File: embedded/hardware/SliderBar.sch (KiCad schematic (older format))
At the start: 35 parts, among them J1 USB_B_Mini, J2 MOTOR_OUT, J3 POT_IN, J4 DEBUG, U1 MIC5205-3.3YM5, U2 TB6612FNG, U3 MT3608, U4 STM32F072C8Tx

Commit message: Change connector footprints to JST GH 1.25mm
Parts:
- J2: footprint Connector_JST:JST_GH_SM02B-GHS-TB_1x02-1MP_P1.25mm_Horizontal -> Connector_Molex:Molex_PicoBlade_53048-0210_1x02_P1.25mm_Horizontal
- J3: footprint Connector_JST:JST_GH_SM03B-GHS-TB_1x03-1MP_P1.25mm_Horizontal -> Connector_Molex:Molex_PicoBlade_53048-0310_1x03_P1.25mm_Horizontal
- J4: footprint Connector_JST:JST_GH_SM05B-GHS-TB_1x05-1MP_P1.25mm_Horizontal -> Connector_Molex:Molex_PicoBlade_53047-0510_1x05_P1.25mm_Vertical
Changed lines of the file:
@@
 F 0 "J4" H 4230 4292 50  0000 L CNN
 F 1 "DEBUG" H 4230 4201 50  0000 L CNN
-F 2 "Connector_JST:JST_GH_SM05B-GHS-TB_1x05-1MP_P1.25mm_Horizontal" H 4150 4250 50  0001 C CNN
+F 2 "Connector_Molex:Molex_PicoBlade_53047-0510_1x05_P1.25mm_Vertical" H 4150 4250 50  0001 C CNN
 F 3 "~" H 4150 4250 50  0001 C CNN
 	1    4150 4250
@@
 F 0 "J2" H 4230 3092 50  0000 L CNN
 F 1 "MOTOR_OUT" H 4230 3001 50  0000 L CNN
-F 2 "Connector_JST:JST_GH_SM02B-GHS-TB_1x02-1MP_P1.25mm_Horizontal" H 4150 3100 50  0001 C CNN
+F 2 "Connector_Molex:Molex_PicoBlade_53048-0210_1x02_P1.25mm_Horizontal" H 4150 3100 50  0001 C CNN
 F 3 "~" H 4150 3100 50  0001 C CNN
 	1    4150 3100
@@
 F 0 "J3" H 4230 3667 50  0000 L CNN
 F 1 "POT_IN" H 4230 3576 50  0000 L CNN
-F 2 "Connector_JST:JST_GH_SM03B-GHS-TB_1x03-1MP_P1.25mm_Horizontal" H 4150 3625 50  0001 C CNN
+F 2 "Connector_Molex:Molex_PicoBlade_53048-0310_1x03_P1.25mm_Horizontal" H 4150 3625 50  0001 C CNN
 F 3 "~" H 4150 3625 50  0001 C CNN
 	1    4150 3625
@@
 NRST
 $Comp
-L power:GND #PWR018
+L power:GND #PWR?
 U 1 1 5BB23C60
 P 3950 4150
-F 0 "#PWR018" H 3950 3900 50  0001 C CNN
+F 0 "#PWR?" H 3950 3900 50  0001 C CNN
 F 1 "GND" V 3950 4000 50  0000 R CNN
 F 2 "" H 3950 4150 50  0001 C CNN
@@
 POT
 $Comp
-L power:GND #PWR020
+L power:GND #PWR?
 U 1 1 5BB24025
 P 3950 3725
-F 0 "#PWR020" H 3950 3475 50  0001 C CNN
+F 0 "#PWR?" H 3950 3475 50  0001 C CNN
 F 1 "GND" H 3955 3552 50  0000 C CNN
 F 2 "" H 3950 3725 50  0001 C CNN
@@
 $EndComp
 $Comp
-L power:+3.3V #PWR019
+L power:+3.3V #PWR?
 U 1 1 5BB24078
 P 3950 3525
-F 0 "#PWR019" H 3950 3375 50  0001 C CNN
+F 0 "#PWR?" H 3950 3375 50  0001 C CNN
 F 1 "+3.3V" H 3965 3698 50  0000 C CNN
 F 2 "" H 3950 3525 50  0001 C CNN
@@
 $EndComp
 $Comp
-L power:GND #PWR05
+L power:GND #PWR?
 U 1 1 5BB24638
 P 9350 6050
-F 0 "#PWR05" H 9350 5800 50  0001 C CNN
+F 0 "#PWR?" H 9350 5800 50  0001 C CNN
 F 1 "GND" H 9355 5877 50  0000 C CNN
 F 2 "" H 9350 6050 50  0001 C CNN
@@
 MOT_IN_PWM
 $Comp
-L power:+10V #PWR07
+L power:+10V #PWR?
 U 1 1 5BB2664B
 P 9950 3450
-F 0 "#PWR07" H 9950 3300 50  0001 C CNN
+F 0 "#PWR?" H 9950 3300 50  0001 C CNN
 F 1 "+10V" H 9965 3623 50  0000 C CNN
 F 2 "" H 9950 3450 50  0001 C CNN
@@
 	9750 3900 9750 3950
 $Comp
-L power:+3V3 #PWR04
+L power:+3V3 #PWR?
 U 1 1 5BB27786
 P 9350 3950
-F 0 "#PWR04" H 9350 3800 50  0001 C CNN
+F 0 "#PWR?" H 9350 3800 50  0001 C CNN
 F 1 "+3V3" H 9300 4100 50  0000 C CNN
 F 2 "" H 9350 3950 50  0001 C CNN
@@
 MOT_IN_2
 $Comp
-L power:GND #PWR010
+L power:GND #PWR?
 U 1 1 5BB27E3D
 P 10400 4000
-F 0 "#PWR010" H 10400 3750 50  0001 C CNN
+F 0 "#PWR?" H 10400 3750 50  0001 C CNN
 F 1 "GND" V 10405 3872 50  0000 R CNN
 F 2 "" H 10400 4000 50  0001 C CNN
@@
 Connection ~ 9950 3900
 $Comp
-L power:+3V3 #PWR016
+L power:+3V3 #PWR?
 U 1 1 5BCA2B2D
 P 6750 1900
-F 0 "#PWR016" H 6750 1750 50  0001 C CNN
+F 0 "#PWR?" H 6750 1750 50  0001 C CNN
 F 1 "+3V3" H 6765 2073 50  0000 C CNN
 F 2 "" H 6750 1900 50  0001 C CNN
@@
 Connection ~ 6650 2000
 $Comp
-L power:GND #PWR015
+L power:GND #PWR?
 U 1 1 5BCAB682
 P 6550 5300
-F 0 "#PWR015" H 6550 5050 50  0001 C CNN
+F 0 "#PWR?" H 6550 5050 50  0001 C CNN
 F 1 "GND" H 6555 5127 50  0000 C CNN
 F 2 "" H 6550 5300 50  0001 C CNN
@@
 Connection ~ 6850 2000
 $Comp
-L power:GND #PWR014
+L power:GND #PWR?
 U 1 1 5BCB754A
 P 5500 2700
-F 0 "#PWR014" H 5500 2450 50  0001 C CNN
+F 0 "#PWR?" H 5500 2450 50  0001 C CNN
 F 1 "GND" H 5505 2527 50  0000 C CNN
 F 2 "" H 5500 2700 50  0001 C CNN
@@
 	2050 1800 2050 1700
 $Comp
-L power:GND #PWR06
+L power:GND #PWR?
 U 1 1 5BD40D38
 P 2050 1800
-F 0 "#PWR06" H 2050 1550 50  0001 C CNN
+F 0 "#PWR?" H 2050 1550 50  0001 C CNN
 F 1 "GND" H 2055 1627 50  0000 C CNN
 F 2 "" H 2050 1800 50  0001 C CNN
@@
 $EndComp
 $Comp
-L power:+3V3 #PWR03
+L power:+3V3 #PWR?
 U 1 1 5BCA296C
 P 1900 1200
-F 0 "#PWR03" H 1900 1050 50  0001 C CNN
+F 0 "#PWR?" H 1900 1050 50  0001 C CNN
 F 1 "+3V3" H 1915 1373 50  0000 C CNN
 F 2 "" H 1900 1200 50  0001 C CNN
@@
 3.3V REGULATOR
 $Comp
-L power:GND #PWR02
+L power:GND #PWR?
 U 1 1 5BC34408
 P 1500 2000
-F 0 "#PWR02" H 1500 1750 50  0001 C CNN
+F 0 "#PWR?" H 1500 1750 50  0001 C CNN
 F 1 "GND" H 1505 1827 50  0000 C CNN
 F 2 "" H 1500 2000 50  0001 C CNN
@@
 Id = sqrt(Iout * Imax)
 $Comp
-L power:GND #PWR012
+L power:GND #PWR?
 U 1 1 5BC4D897
 P 2850 3850
-F 0 "#PWR012" H 2850 3600 50  0001 C CNN
+F 0 "#PWR?" H 2850 3600 50  0001 C CNN
 F 1 "GND" H 2855 3677 50  0000 C CNN
 F 2 "" H 2850 3850 50  0001 C CNN
@@
 Recommended:\n4.7uH - 22uH
 $Comp
-L power:GND #PWR011
+L power:GND #PWR?
 U 1 1 5BC48783
 P 2150 4450
-F 0 "#PWR011" H 2150 4200 50  0001 C CNN
+F 0 "#PWR?" H 2150 4200 50  0001 C CNN
 F 1 "GND" H 2155 4277 50  0000 C CNN
 F 2 "" H 2150 4450 50  0001 C CNN
@@
 $EndComp
 $Comp
-L power:+10V #PWR013
+L power:+10V #PWR?
 U 1 1 5BC3AC64
 P 2850 3250
-F 0 "#PWR013" H 2850 3100 50  0001 C CNN
+F 0 "#PWR?" H 2850 3100 50  0001 C CNN
 F 1 "+10V" H 2865 3423 50  0000 C CNN
 F 2 "" H 2850 3250 50  0001 C CNN
@@
 $EndComp
 $Comp
-L power:GND #PWR09
+L power:GND #PWR?
 U 1 1 5BC3A8CB
 P 900 4050
-F 0 "#PWR09" H 900 3800 50  0001 C CNN
+F 0 "#PWR?" H 900 3800 50  0001 C CNN
 F 1 "GND" H 905 3877 50  0000 C CNN
 F 2 "" H 900 4050 50  0001 C CNN
@@
 Connection ~ 9950 3550
 $Comp
-L power:+5V #PWR017
+L power:+5V #PWR?
 U 1 1 5BD9F21E
 P 1100 1200
-F 0 "#PWR017" H 1100 1050 50  0001 C CNN
+F 0 "#PWR?" H 1100 1050 50  0001 C CNN
 F 1 "+5V" H 1115 1373 50  0000 C CNN
 F 2 "" H 1100 1200 50  0001 C CNN
@@
 $EndComp
 $Comp
-L power:+5V #PWR01
+L power:+5V #PWR?
 U 1 1 5BD9F4E9
 P 900 3250
-F 0 "#PWR01" H 900 3100 50  0001 C CNN
+F 0 "#PWR?" H 900 3100 50  0001 C CNN
 F 1 "+5V" H 915 3423 50  0000 C CNN
 F 2 "" H 900 3250 50  0001 C CNN
@@
 $EndComp
 $Comp
-L power:VBUS #PWR023
+L power:VBUS #PWR?
 U 1 1 5BD9F98D
 P 3000 1300
-F 0 "#PWR023" H 3000 1150 50  0001 C CNN
+F 0 "#PWR?" H 3000 1150 50  0001 C CNN
 F 1 "VBUS" H 3015 1473 50  0000 C CNN
 F 2 "" H 3000 1300 50  0001 C CNN
@@
 $EndComp
 $Comp
-L power:+5V #PWR027
+L power:+5V #PWR?
 U 1 1 5BD9FC3F
 P 3750 1200
-F 0 "#PWR027" H 3750 1050 50  0001 C CNN
+F 0 "#PWR?" H 3750 1050 50  0001 C CNN
 F 1 "+5V" H 3765 1373 50  0000 C CNN
 F 2 "" H 3750 1200 50  0001 C CNN
@@
 $EndComp
 $Comp
-L power:GND #PWR028
+L power:GND #PWR?
 U 1 1 5BDBF2FB
 P 3750 2200
-F 0 "#PWR028" H 3750 1950 50  0001 C CNN
+F 0 "#PWR?" H 3750 1950 50  0001 C CNN
 F 1 "GND" H 3755 2027 50  0000 C CNN
 F 2 "" H 3750 2200 50  0001 C CNN
@@
 USB_DP
 $Comp
-L power:GND #PWR08
+L power:GND #PWR?
 U 1 1 5BDDF695
 P 950 6400
-F 0 "#PWR08" H 950 6150 50  0001 C CNN
+F 0 "#PWR?" H 950 6150 50  0001 C CNN
 F 1 "GND" H 955 6227 50  0000 C CNN
 F 2 "" H 950 6400 50  0001 C CNN
@@
 Connection ~ 10400 3900
 $Comp
-L power:VPP #PWR029
+L power:VPP #PWR?
 U 1 1 5BD8AB17
 P 3950 4350
-F 0 "#PWR029" H 3950 4200 50  0001 C CNN
+F 0 "#PWR?" H 3950 4200 50  0001 C CNN
 F 1 "VPP" V 3950 4650 50  0000 R CNN
 F 2 "" H 3950 4350 50  0001 C CNN
@@
 $EndComp
 $Comp
-L power:VPP #PWR024
+L power:VPP #PWR?
 U 1 1 5BD8AD8C
 P 3000 1650
-F 0 "#PWR024" H 3000 1500 50  0001 C CNN
+F 0 "#PWR?" H 3000 1500 50  0001 C CNN
 F 1 "VPP" H 3015 1823 50  0000 C CNN
 F 2 "" H 3000 1650 50  0001 C CNN
@@
 	4750 2700 3400 2700
 $Comp
-L power:VBUS #PWR021
+L power:VBUS #PWR?
 U 1 1 5BE0AEED
 P 1450 5500
-F 0 "#PWR021" H 1450 5350 50  0001 C CNN
+F 0 "#PWR?" H 1450 5350 50  0001 C CNN
 F 1 "VBUS" H 1465 5673 50  0000 C CNN
 F 2 "" H 1450 5500 50  0001 C CNN
@@
 Connection ~ 1050 6300
 $Comp
-L power:+3V3 #PWR022
+L power:+3V3 #PWR?
 U 1 1 5BE2449C
 P 1750 5400
-F 0 "#PWR022" H 1750 5250 50  0001 C CNN
+F 0 "#PWR?" H 1750 5250 50  0001 C CNN
 F 1 "+3V3" H 1765 5573 50  0000 C CNN
 F 2 "" H 1750 5400 50  0001 C CNN
@@
 	10900 2950 10900 6300
 $Comp
-L power:+3V3 #PWR025
+L power:+3V3 #PWR?
 U 1 1 5BE61DFB
 P 3650 6800
-F 0 "#PWR025" H 3650 6650 50  0001 C CNN
+F 0 "#PWR?" H 3650 6650 50  0001 C CNN
 F 1 "+3V3" H 3665 6973 50  0000 C CNN
 F 2 "" H 3650 6800 50  0001 C CNN
@@
 $EndComp
 $Comp
-L power:GND #PWR026
+L power:GND #PWR?
 U 1 1 5BE61E6A
 P 3650 7400
-F 0 "#PWR026" H 3650 7150 50  0001 C CNN
+F 0 "#PWR?" H 3650 7150 50  0001 C CNN
 F 1 "GND" H 3655 7227 50  0000 C CNN
 F 2 "" H 3650 7400 50  0001 C CNN
@@
 $EndComp
 $Comp
-L power:GND #PWR031
+L power:GND #PWR?
 U 1 1 5BE61EC4
 P 5500 7400
-F 0 "#PWR031" H 5500 7150 50  0001 C CNN
+F 0 "#PWR?" H 5500 7150 50  0001 C CNN
 F 1 "GND" H 5505 7227 50  0000 C CNN
 F 2 "" H 5500 7400 50  0001 C CNN
@@
 $EndComp
 $Comp
-L power:GND #PWR034
+L power:GND #PWR?
 U 1 1 5BE61F1E
 P 6150 7400
-F 0 "#PWR034" H 6150 7150 50  0001 C CNN
+F 0 "#PWR?" H 6150 7150 50  0001 C CNN
 F 1 "GND" H 6155 7227 50  0000 C CNN
 F 2 "" H 6150 7400 50  0001 C CNN
@@
 $EndComp
 $Comp
-L power:+5V #PWR030
+L power:+5V #PWR?
 U 1 1 5BE6210E
 P 5500 6800
-F 0 "#PWR030" H 5500 6650 50  0001 C CNN
+F 0 "#PWR?" H 5500 6650 50  0001 C CNN
 F 1 "+5V" H 5515 6973 50  0000 C CNN
 F 2 "" H 5500 6800 50  0001 C CNN
@@
 $EndComp
 $Comp
-L power:+10V #PWR033
+L power:+10V #PWR?
 U 1 1 5BE621BC
 P 6150 6800
-F 0 "#PWR033" H 6150 6650 50  0001 C CNN
+F 0 "#PWR?" H 6150 6650 50  0001 C CNN
 F 1 "+10V" H 6165 6973 50  0000 C CNN
 F 2 "" H 6150 6800 50  0001 C CNN
@@
 NOT NEEDED
 $Comp
-L power:GND #PWR032
+L power:GND #PWR?
 U 1 1 5BEDB912
 P 5850 2900
-F 0 "#PWR032" H 5850 2650 50  0001 C CNN
+F 0 "#PWR?" H 5850 2650 50  0001 C CNN
 F 1 "GND" H 5855 2727 50  0000 C CNN
 F 2 "" H 5850 2900 50  0001 C CNN

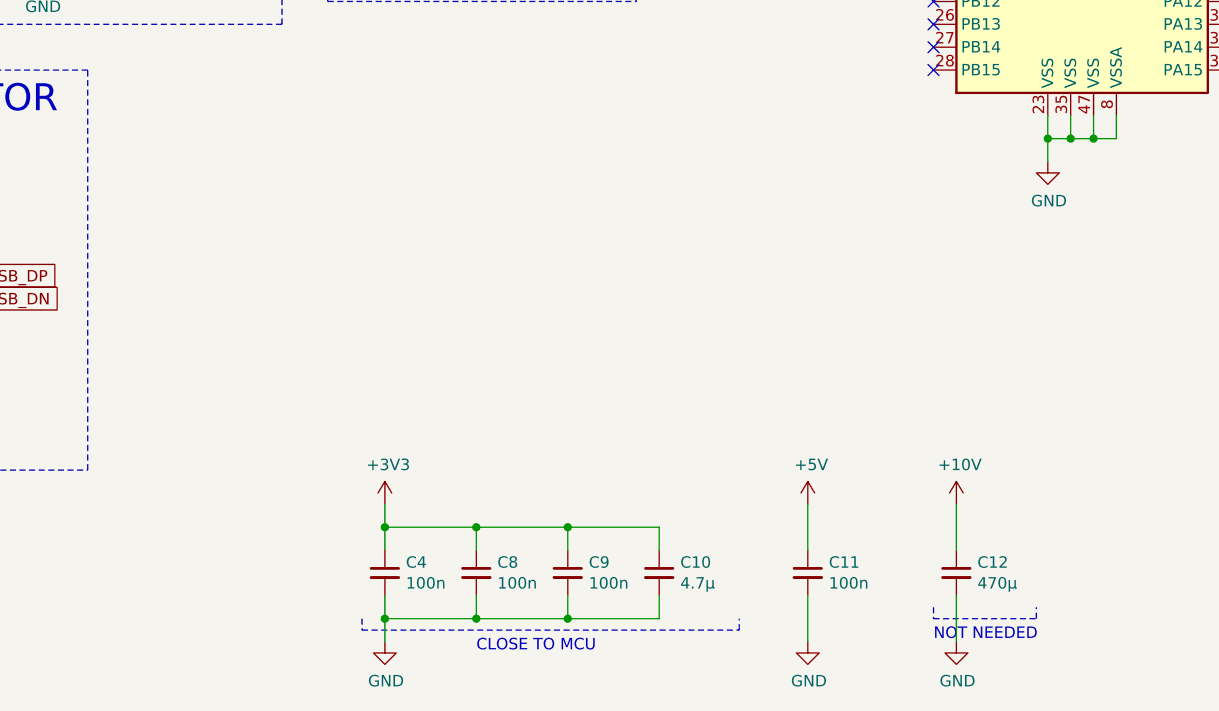
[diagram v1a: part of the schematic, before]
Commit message: Fix lot of footprints, Add mounting holes
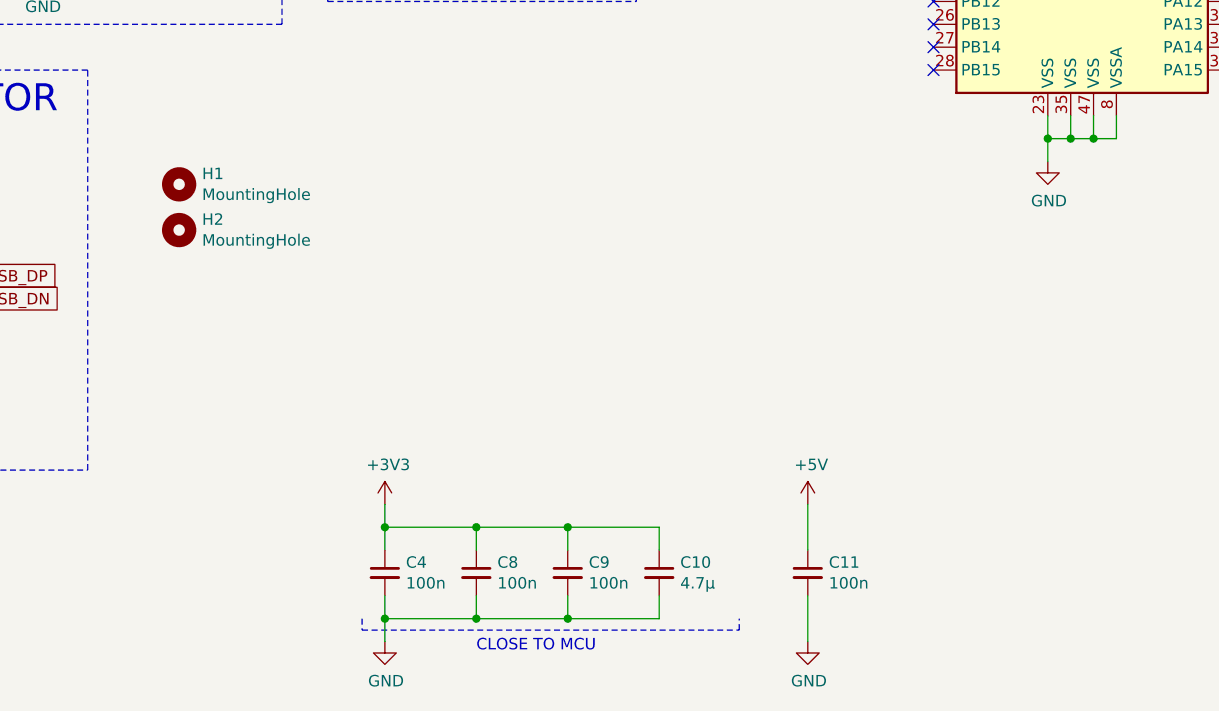
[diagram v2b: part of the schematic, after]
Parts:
- removed C12: 470µ, Capacitor_SMD:C_1206_3216Metric_Pad1.42x1.75mm_HandSolder, symbol Device:C_Small
- added H1, H2: MountingHole, MountingHole:MountingHole_3.2mm_M3_ISO14580, symbol Mechanical:MountingHole
- L1: footprint Inductor_SMD:L_1206_3216Metric_Pad1.42x1.75mm_HandSolder -> Inductor_SMD:L_7.3x7.3_H3.5
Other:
- note removed: "NOT NEEDED"
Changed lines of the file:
@@
 F 0 "L1" V 1472 3350 50  0000 C CNN
 F 1 "4.7µ" V 1563 3350 50  0000 C CNN
-F 2 "Inductor_SMD:L_1206_3216Metric_Pad1.42x1.75mm_HandSolder" H 1650 3350 50  0001 C CNN
+F 2 "Inductor_SMD:L_7.3x7.3_H3.5" H 1650 3350 50  0001 C CNN
 F 3 "~" H 1650 3350 50  0001 C CNN
 	1    1650 3350
@@
 $EndComp
 $Comp
-L power:GND #PWR?
-U 1 1 5BE61F1E
-P 6150 7400
-F 0 "#PWR?" H 6150 7150 50  0001 C CNN
-F 1 "GND" H 6155 7227 50  0000 C CNN
-F 2 "" H 6150 7400 50  0001 C CNN
-F 3 "" H 6150 7400 50  0001 C CNN
-	1    6150 7400
-	1    0    0    -1
-$EndComp
-$Comp
 L power:+5V #PWR?
 U 1 1 5BE6210E
@@
 $EndComp
 $Comp
-L power:+10V #PWR?
-U 1 1 5BE621BC
-P 6150 6800
-F 0 "#PWR?" H 6150 6650 50  0001 C CNN
-F 1 "+10V" H 6165 6973 50  0000 C CNN
-F 2 "" H 6150 6800 50  0001 C CNN
-F 3 "" H 6150 6800 50  0001 C CNN
-	1    6150 6800
-	1    0    0    -1
-$EndComp
-$Comp
 L Device:C_Small C4
 U 1 1 5BE62B6A
@@
 Wire Wire Line
 	5500 7000 5500 6800
-$Comp
-L Device:C_Small C12
-U 1 1 5BEB3209
-P 6150 7100
-F 0 "C12" H 6242 7146 50  0000 L CNN
-F 1 "470µ" H 6242 7055 50  0000 L CNN
-F 2 "Capacitor_SMD:C_1206_3216Metric_Pad1.42x1.75mm_HandSolder" H 6150 7100 50  0001 C CNN
-F 3 "~" H 6150 7100 50  0001 C CNN
-	1    6150 7100
-	1    0    0    -1
-$EndComp
-Wire Wire Line
-	6150 6800 6150 7000
-Wire Wire Line
-	6150 7200 6150 7400
-Wire Notes Line width 12 style solid
-	6050 7250 6050 7300
-Wire Notes Line width 12 style solid
-	6050 7300 6500 7300
-Wire Notes Line width 12 style solid
-	6500 7300 6500 7250
-Text Notes 6050 7400 0    50   ~ 0
-NOT NEEDED
 $Comp
 L power:GND #PWR?
@@
 Text Label 1350 5900 0    50   ~ 0
 D-
+$Comp
+L Mechanical:MountingHole H1
+U 1 1 5BDC03AF
+P 2750 5400
+F 0 "H1" H 2850 5446 50  0000 L CNN
+F 1 "MountingHole" H 2850 5355 50  0000 L CNN
+F 2 "MountingHole:MountingHole_3.2mm_M3_ISO14580" H 2750 5400 50  0001 C CNN
+F 3 "~" H 2750 5400 50  0001 C CNN
+	1    2750 5400
+	1    0    0    -1
+$EndComp
+$Comp
+L Mechanical:MountingHole H2
+U 1 1 5BDC0899
+P 2750 5600
+F 0 "H2" H 2850 5646 50  0000 L CNN
+F 1 "MountingHole" H 2850 5555 50  0000 L CNN
+F 2 "MountingHole:MountingHole_3.2mm_M3_ISO14580" H 2750 5600 50  0001 C CNN
+F 3 "~" H 2750 5600 50  0001 C CNN
+	1    2750 5600
+	1    0    0    -1
+$EndComp
 $EndSCHEMATC
